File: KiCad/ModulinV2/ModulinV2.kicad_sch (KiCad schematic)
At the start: 1 part

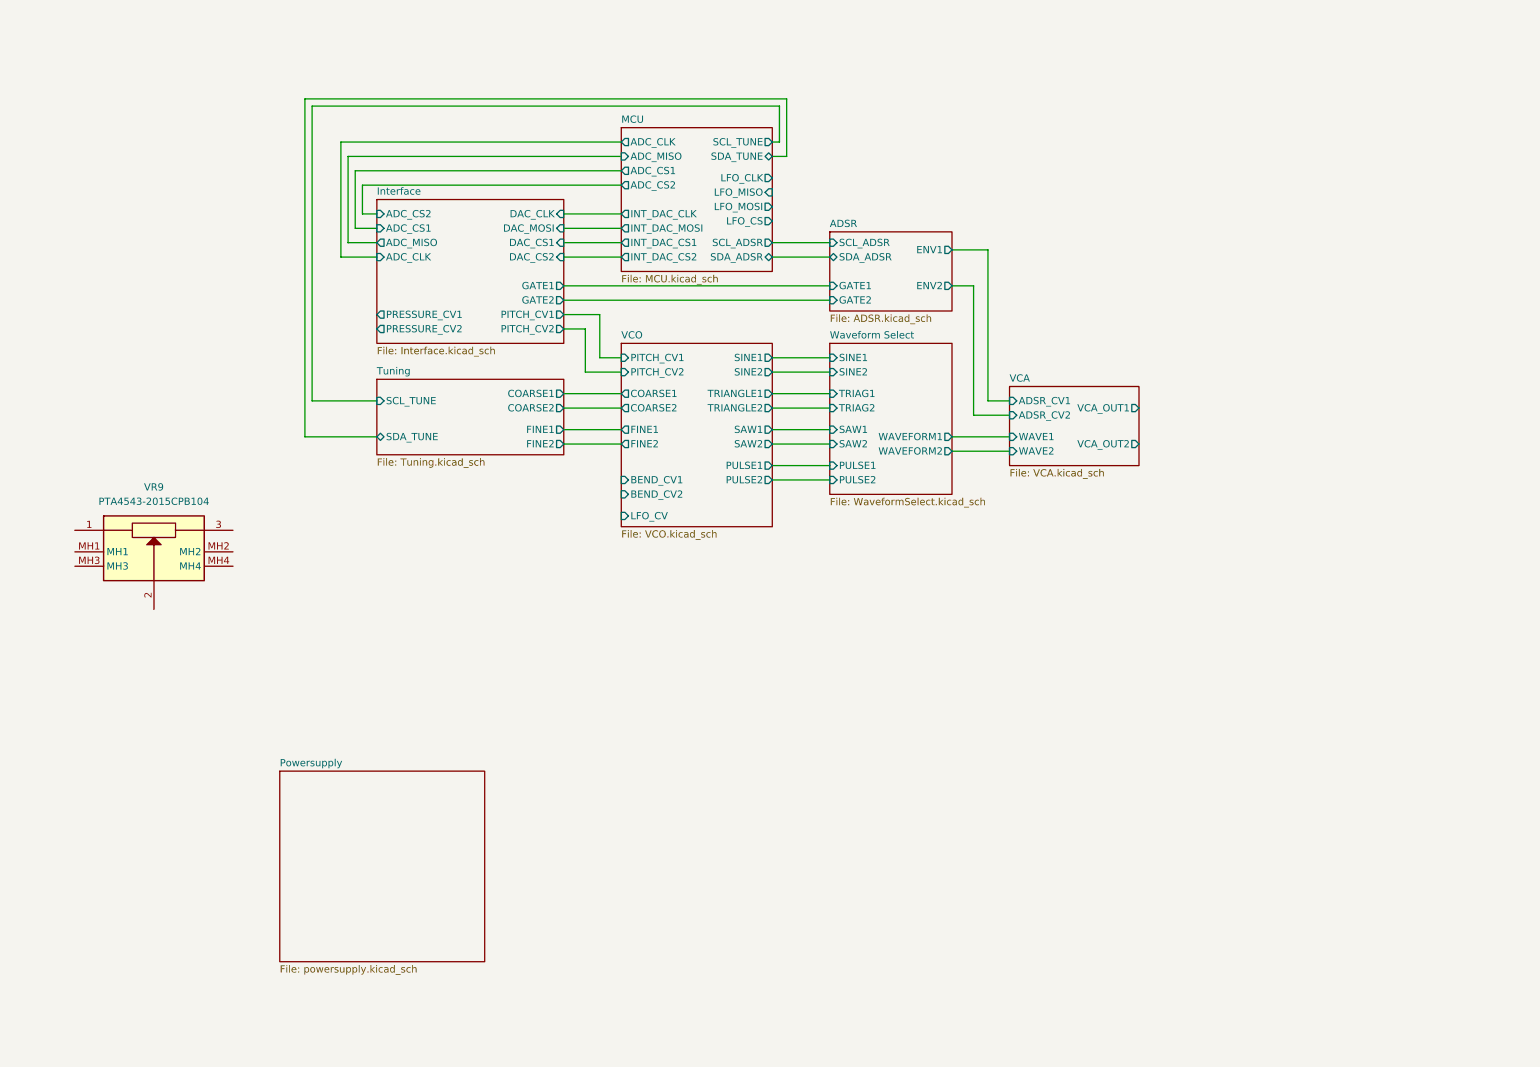
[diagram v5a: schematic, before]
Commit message: Modified supply schematic and made modulation wheel initial design
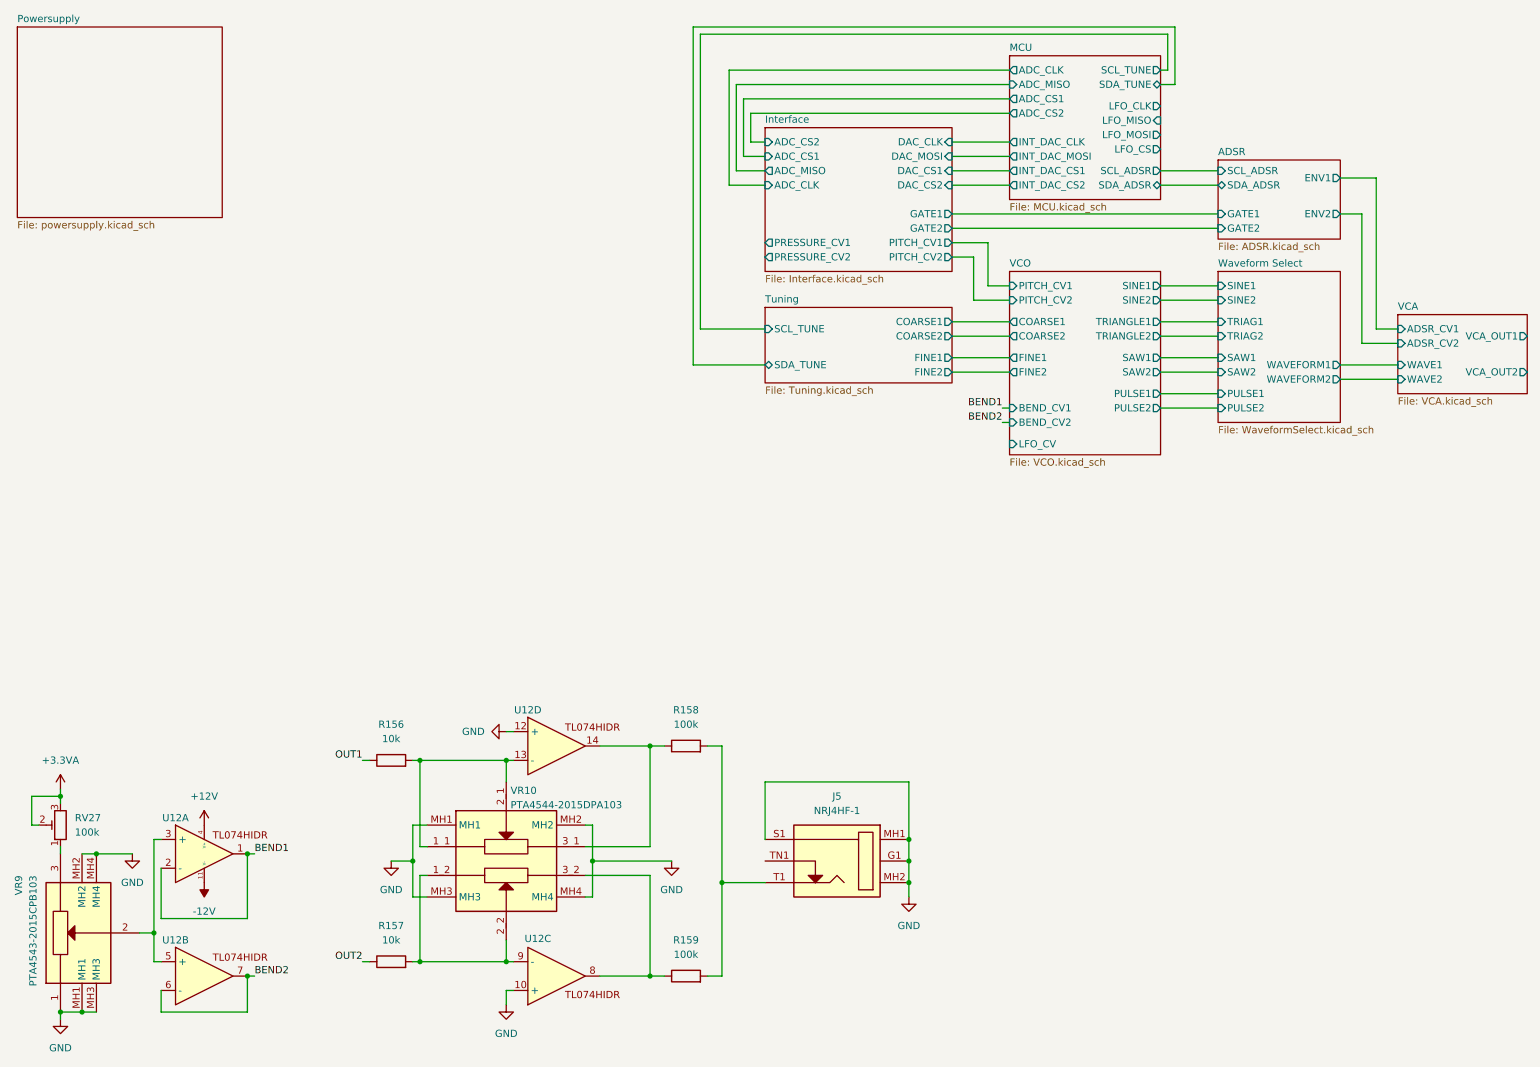
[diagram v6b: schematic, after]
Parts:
- removed VR9: PTA4543-2015CPB104, PTA45432015CPB503, symbol PTA4543-2015CPB104:PTA4543-2015CPB104
- added J5: NRJ4HF-1, NRJ4HF1, symbol NRJ4HF-1:NRJ4HF-1
- added R156, R157: 10k, symbol Device:R
- added R158, R159: 100k, symbol Device:R
- added RV27: 100k, symbol Device:R_Potentiometer_Trim
- added U12: ~, symbol TL074HIDR:TL074HIDRx4
- added VR10: PTA4544-2015DPA103, symbol PTA4544-2015DPA103:PTA4544-2015DPA103
- added VR9: PTA4543-2015CPB103, PTA45432015CPB503, symbol PTA4543-2015CPB104:PTA4543-2015CPB103
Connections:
- new net: R157.2, U12.9 (-), VR10.1_2, VR10.2_2
- new net: RV27.1, VR9.3
- new net: U12.3 (+), U12.5 (+), VR9.2
- new net: R156.2, U12.13 (-), VR10.1_1, VR10.2_1
- new net: R159.1, U12.8, VR10.3_2
- new net: R158.1, U12.14, VR10.3_1
- new net: J5.T1, R158.2, R159.2
- new net +12V: U12.4 (V+)
- new net +3.3VA: RV27.2, RV27.3
- new net -12V: U12.11 (V-)
- new net BEND1: U12.1, U12.2 (-)
- new net BEND2: U12.6 (-), U12.7
- new net GND: J5.G1, J5.MH1, J5.MH2, J5.S1, U12.10 (+), U12.12 (+), VR10.MH1, VR10.MH2, VR10.MH3, VR10.MH4, VR9.1, VR9.MH1, VR9.MH2, VR9.MH3, VR9.MH4
- new net OUT1: R156.1
- new net OUT2: R157.1
